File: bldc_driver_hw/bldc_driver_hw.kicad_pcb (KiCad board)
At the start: 2 copper layers, 100 x 150 mm, 282 parts, among them J1 Conn_01x02, J2 USB_C_Receptacle_USB2.0_16P, J3 JTAG_CONN, J4 USB_C_Receptacle_USB2.0_16P, J5 Conn_01x03_Pin, J6 Conn_01x03_Pin, J7 Conn_01x03, J9 Conn_01x02, Q1 IPB026N06NATMA1, Q2 IPB026N06NATMA1, Q3 IPB026N06NATMA1, Q4 IPB026N06NATMA1, Q5 IPB026N06NATMA1, Q6 IPB026N06NATMA1, SW1 SW_Push, SW2 SW_Push, SW3 SW_Push, U10 INA240A1D, U11 INA240A1D, U12 SN65HVD234, U13 MCP6569, U14 TPS54360DDA, U15 UCC27288, U16 UCC27288, U17 UCC27288, U2 USBLC6-2SC6, U3 TPS562201DDCR, U4 AMS1117-3.3, U5 MCP1501-33xSN, U6 STM32G474RETx, U7 USBLC6-2SC6, U8 ESP32-C6-MINI-1, U9 INA240A1D, Y1 24MHz

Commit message: board finished
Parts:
- added C1: 47uF, Capacitor_Tantalum_SMD:CP_EIA-6032-15_Kemet-U, F.Cu at (108.6, 25.6)
- added JP1: SolderJumper_2_Open, Jumper:SolderJumper-2_P1.3mm_Open_Pad1.0x1.5mm, F.Cu at (127.5, 162.2)
- added R17: 10k, Resistor_SMD:R_0402_1005Metric, F.Cu at (145.6, 48.3)
- added R19: 10k, Resistor_SMD:R_0402_1005Metric, F.Cu at (145.6, 50.4)
- moved D6 5.04 mm to (109.5, 32.0)
- moved D5 1.80 mm to (109.5, 30.3)
- moved C49 0.10 mm to (111.5, 23.8)
- moved C50 0.10 mm to (113.1, 23.8)
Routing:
- net +48V: track 49.4 -> 60.6 mm
- net VDD: track 32.8 -> 43.0 mm
- net +3.3V: track 503.7 -> 510.2 mm, vias 29 -> 32
- net Net-(D6-A): track 1.65 -> 6.92 mm
- net Net-(JP9-A): track 31.7 -> 34.6 mm
- net /CAN_TRANSCIEVER/CAN_EN: track 46.4 -> 48.6 mm
- net GND: track 116.9 -> 118.0 mm, vias 804 -> 793
- net Net-(D5-A): track 1.64 -> 2.36 mm
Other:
- board text added: "PHASE U"
- board text added: "PHASE V"
- board text added: "PHASE W"
- board text removed: "Designed by Tetes & Żak"

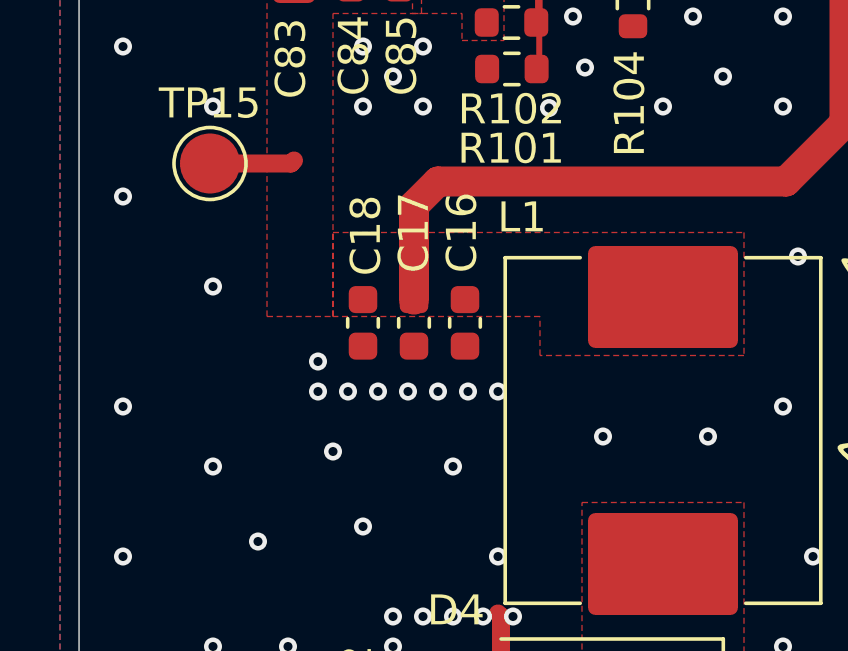
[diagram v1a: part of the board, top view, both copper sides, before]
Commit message: added lcsc codes
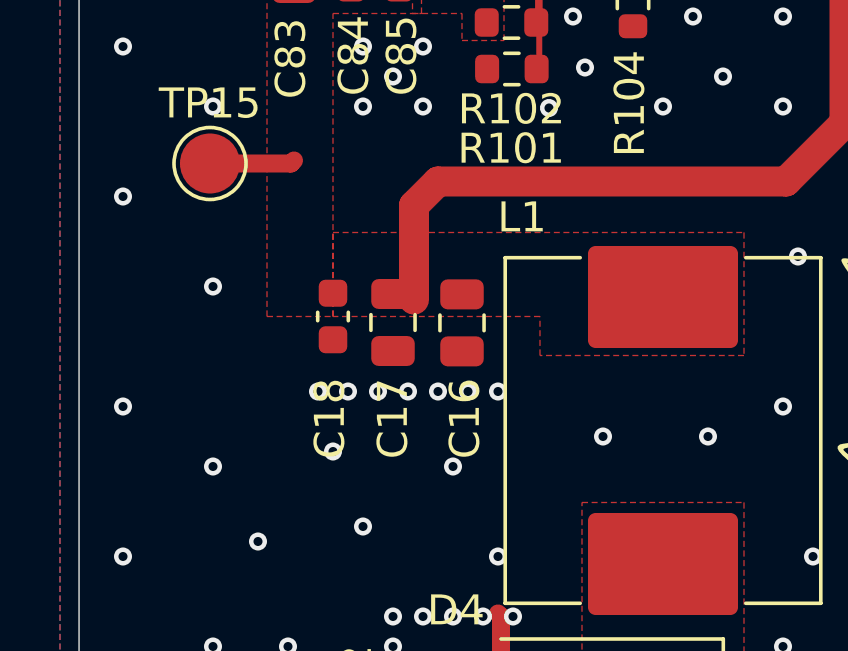
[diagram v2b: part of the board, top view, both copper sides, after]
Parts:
- C16, C17: footprint Capacitor_SMD:C_0603_1608Metric -> Capacitor_SMD:C_0805_2012Metric
- R66, R67, R68, R69, R70, R71: value R_FILTER -> 0R
- moved C18 1.02 mm to (115.0, 127.0)
- moved C17 0.70 mm to (117.0, 127.2)
- moved C16 0.10 mm to (119.3, 127.2)
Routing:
- net GND: vias 793 -> 792

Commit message: finished_board
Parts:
- added G***: LOGO, bldc_driver_footprint:disgned, F.Cu at (137.4, 107.0)
- C6: value 6.8pF -> 10pF
- C7: value 1.8nF -> 2.2nF; footprint Capacitor_SMD:C_0603_1608Metric -> Capacitor_SMD:C_0805_2012Metric
- D1, D11, D12, D15, D16, D2, D20, D21, D22, D3, D7, D8: value SS24 -> SS54
- R12: value 44.2k -> 47k
- R33, R34, R44, R45, R55, R56: value 35R -> 33R
- R35, R36, R46, R47, R57, R58: value R_GATE -> 0R
- R92, R93, R94: value R_Small -> 0R
- R95, R96, R97: value R_Small -> 510k
- moved TP8 6.44 mm to (108.2, 153.9)
- moved J1 3.69 mm to (119.3, 159.6), turned to 0 degrees
- moved J9 2.00 mm to (189.0, 157.7)
- moved C40 2.00 mm to (174.0, 159.0)
- moved C39 1.00 mm to (156.0, 159.0)
- moved J7 0.57 mm to (148.1, 18.5)
- moved C7 0.20 mm to (132.0, 144.6)
- turned R35 to 180 degrees
- turned R46 to 180 degrees
- turned R57 to 180 degrees
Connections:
- J7 pad 1: /CAN_TRANSCIEVER/CAN_L -> GND
- J7 pad 2: /CAN_TRANSCIEVER/CAN_H -> /CAN_TRANSCIEVER/CAN_L
- J7 pad 3: GND -> /CAN_TRANSCIEVER/CAN_H
- R35 pad 1: Net-(D7-A) -> Net-(Q1-G)
- R35 pad 2: Net-(Q1-G) -> Net-(D7-A)
- R46 pad 1: Net-(D11-A) -> Net-(Q3-G)
- R46 pad 2: Net-(Q3-G) -> Net-(D11-A)
- R57 pad 1: Net-(D15-A) -> Net-(Q5-G)
- R57 pad 2: Net-(Q5-G) -> Net-(D15-A)
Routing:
- net GND: track 118.0 -> 138.4 mm, vias 792 -> 777
- net VDD: track 43.0 -> 46.4 mm
- net /CAN_TRANSCIEVER/CAN_L: track 12.3 -> 9.58 mm
- net /BEMF_SENS/PHASE_U: track 87.8 -> 89.9 mm
- net /CAN_TRANSCIEVER/CAN_H: track 10.9 -> 9.46 mm
- net /MOTOR_CTRL/CSA/CSA_P: track 39.5 -> 38.8 mm
- net +48V: vias 115 -> 125
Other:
- board text added: "VM"

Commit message: finished
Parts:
- removed R17, R19: 10k, Resistor_SMD:R_0402_1005Metric
- C16, C17: value 47uF -> 22uF
- moved H6 5.14 mm to (157.9, 53.6)
- moved TP23 5.06 mm to (163.0, 55.0)
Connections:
- J3 pad 7: /MCU/JTRST -> /JTCK_SWCLK
- R8 pad 1: /MCU/JTRST -> /JTCK_SWCLK
- U6 pad 57: /MCU/JTRST -> /JTCK_SWCLK
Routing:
- net /MCU/JTRST: track 28.7 -> 0.00 mm, vias 1 -> 0
- net /JTCK_SWCLK: track 14.7 -> 43.5 mm, vias 1 -> 2
- net GND: track 138.4 -> 167.1 mm, vias 777 -> 780
- net +3.3V: track 510.4 -> 505.9 mm, vias 32 -> 30
- net Net-(JP9-A): track 34.6 -> 31.7 mm
- net /CAN_TRANSCIEVER/CAN_EN: track 48.6 -> 46.1 mm
- net /MCU/ADC_CSA_U: track 67.9 -> 69.1 mm
